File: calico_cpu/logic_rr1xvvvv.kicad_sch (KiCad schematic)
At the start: 8 parts, among them U36 74HC08, U37 74HC08, U38 74HC283, U39 74HC283

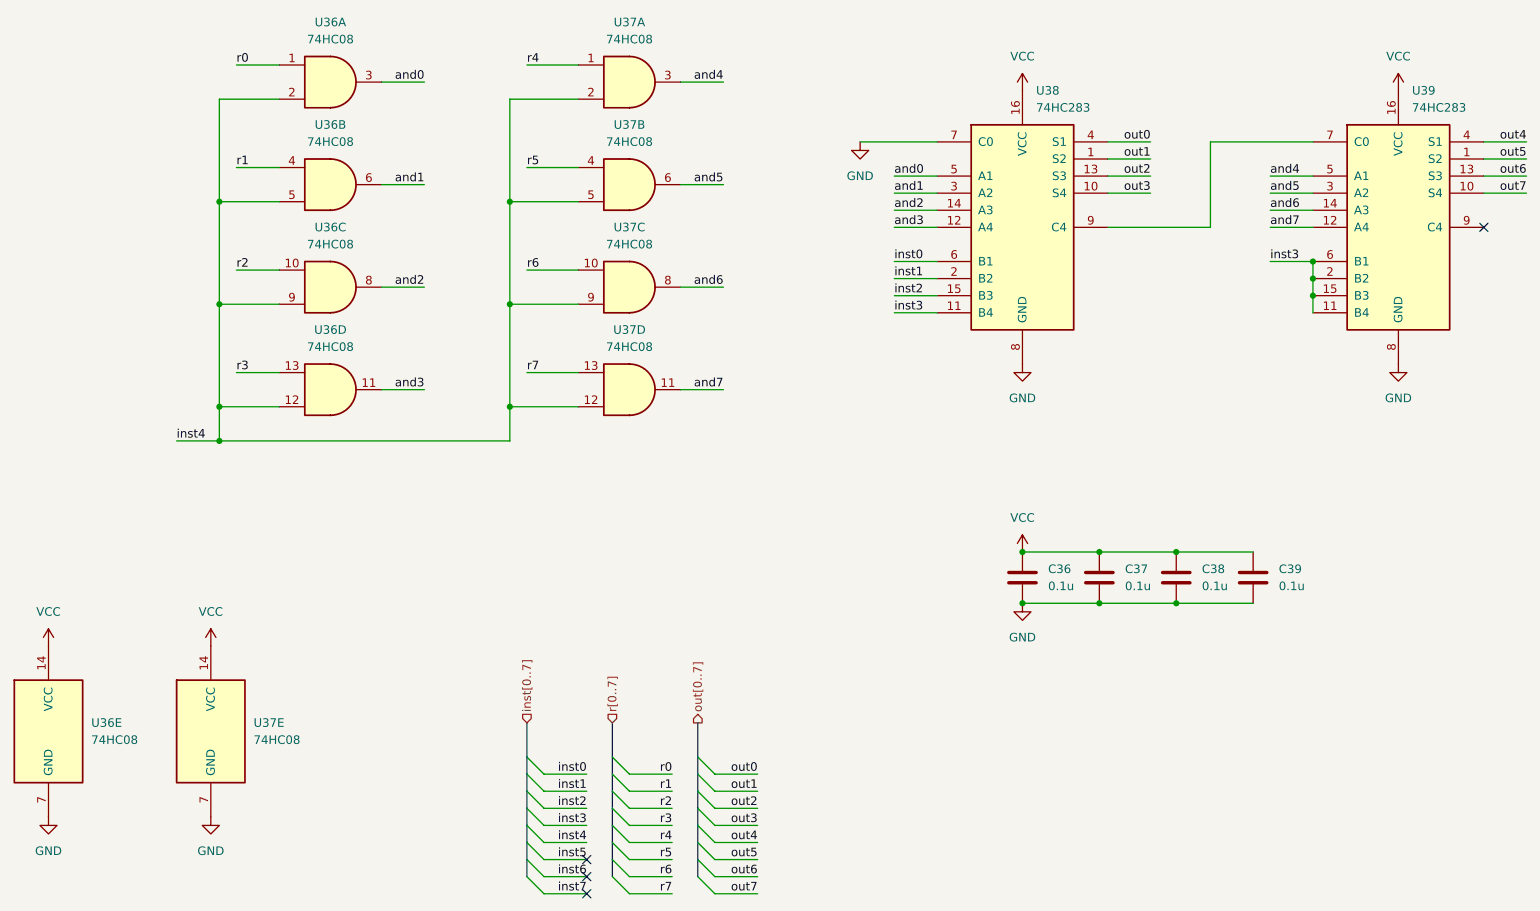
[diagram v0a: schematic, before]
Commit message: change "set immediate" to use zero-extend
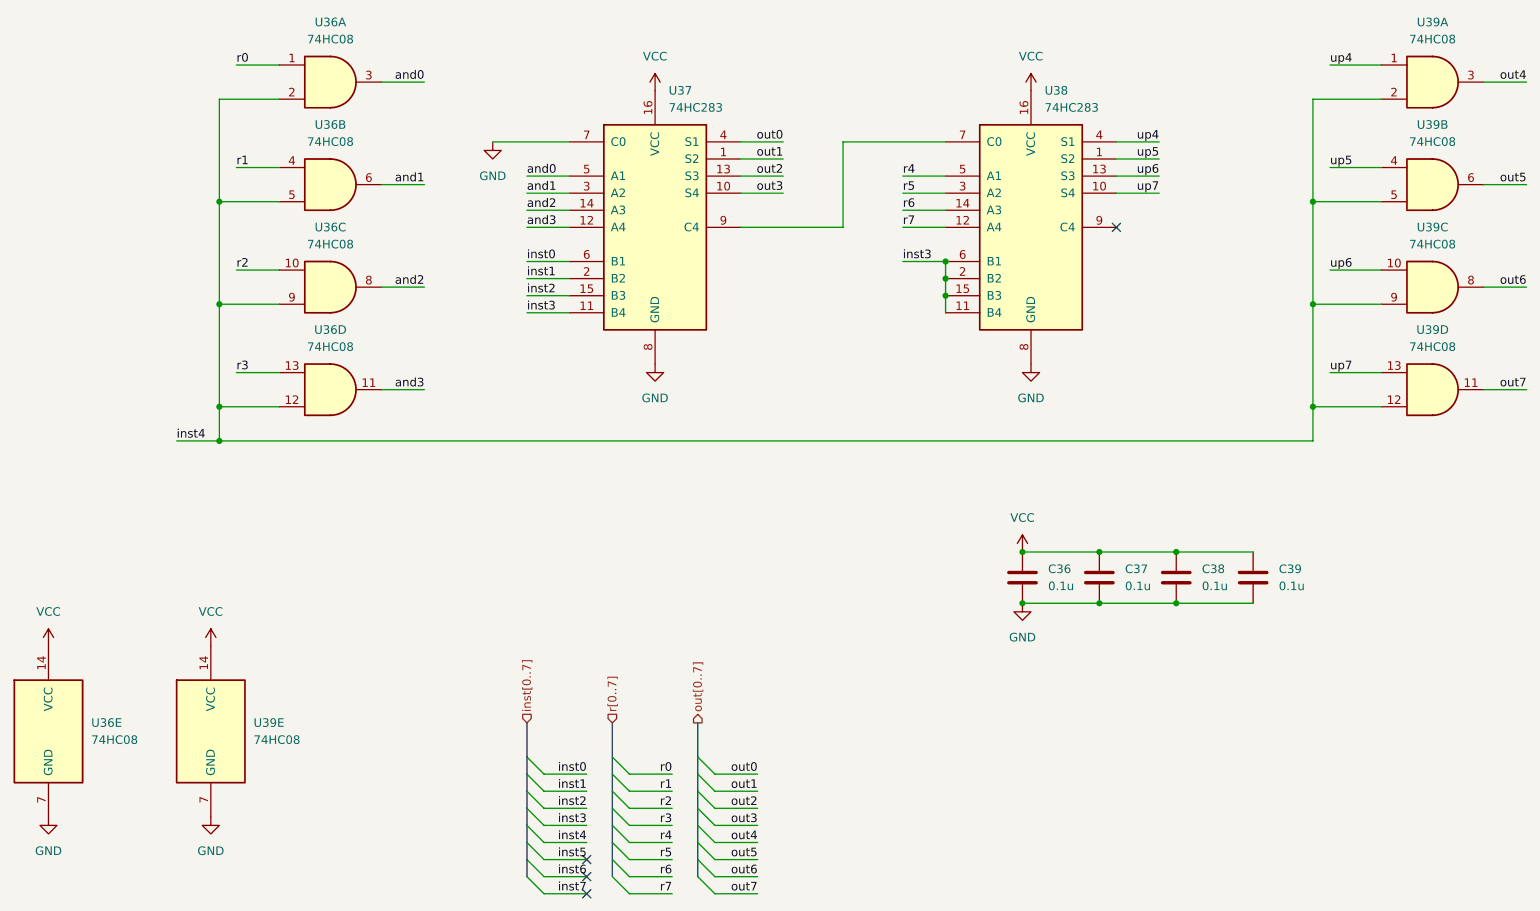
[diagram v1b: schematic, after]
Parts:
- renumbered U38 to U37, U39 to U38, U37 to U39
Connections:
- net out4: now also U39.3; no longer U38.4 (S1)
- net out5: now also U39.6; no longer U38.1 (S2)
- net out6: now also U39.8; no longer U38.13 (S3)
- net out7: now also U39.11; no longer U38.10 (S4)
- net r4: now also U38.5 (A1); no longer U39.1
- net r5: now also U38.3 (A2); no longer U39.4
- net r6: now also U38.14 (A3); no longer U39.10
- net r7: now also U38.12 (A4); no longer U39.13
- removed net and4: U38.5 (A1), U39.3
- removed net and5: U38.3 (A2), U39.6
- removed net and6: U38.14 (A3), U39.8
- removed net and7: U38.12 (A4), U39.11
- new net up4: U38.4 (S1), U39.1
- new net up5: U38.1 (S2), U39.4
- new net up6: U38.13 (S3), U39.10
- new net up7: U38.10 (S4), U39.13
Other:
- moved on the sheet: U37, U38, U39A, U39B, U39C, U39D

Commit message: calico_cpu: assign footprints
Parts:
- C36, C37, C38, C39: footprint (none) -> Capacitor_SMD:C_0805_2012Metric_Pad1.18x1.45mm_HandSolder
- U36, U39: footprint (none) -> PrjLibrary:DIP-14_W7.62mm_D1mm
- U37, U38: footprint (none) -> PrjLibrary:DIP-16_W7.62mm_D1mm
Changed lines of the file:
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@@
     (property "Reference" "U39" (id 0) (at 247.65 90.17 0))
     (property "Value" "74HC08" (id 1) (at 247.65 92.71 0))
-    (property "Footprint" "" (id 2) (at 247.65 99.06 0)
+    (property "Footprint" "PrjLibrary:DIP-14_W7.62mm_D1mm" (id 2) (at 247.65 99.06 0)
       (effects (font (size 1.27 1.27)) hide)
     )
@@
       (effects (font (size 1.27 1.27)) (justify left))
     )
-    (property "Footprint" "" (id 2) (at 199.0852 146.05 0)
+    (property "Footprint" "Capacitor_SMD:C_0805_2012Metric_Pad1.18x1.45mm_HandSolder" (id 2) (at 199.0852 146.05 0)
       (effects (font (size 1.27 1.27)) hide)
     )
@@
       (effects (font (size 1.27 1.27)) (justify left))
     )
-    (property "Footprint" "" (id 2) (at 221.9452 146.05 0)
+    (property "Footprint" "Capacitor_SMD:C_0805_2012Metric_Pad1.18x1.45mm_HandSolder" (id 2) (at 221.9452 146.05 0)
       (effects (font (size 1.27 1.27)) hide)
     )
@@
       (effects (font (size 1.27 1.27)) (justify left))
     )
-    (property "Footprint" "" (id 2) (at 187.6552 146.05 0)
+    (property "Footprint" "Capacitor_SMD:C_0805_2012Metric_Pad1.18x1.45mm_HandSolder" (id 2) (at 187.6552 146.05 0)
       (effects (font (size 1.27 1.27)) hide)
     )
@@
       (effects (font (size 1.27 1.27)) (justify left))
     )
-    (property "Footprint" "" (id 2) (at 66.04 165.1 0)
+    (property "Footprint" "PrjLibrary:DIP-14_W7.62mm_D1mm" (id 2) (at 66.04 165.1 0)
       (effects (font (size 1.27 1.27)) hide)
     )
@@
       (effects (font (size 1.27 1.27)) (justify left))
     )
-    (property "Footprint" "" (id 2) (at 132.08 90.17 0)
+    (property "Footprint" "PrjLibrary:DIP-16_W7.62mm_D1mm" (id 2) (at 132.08 90.17 0)
       (effects (font (size 1.27 1.27)) hide)
     )
@@
     (property "Reference" "U39" (id 0) (at 247.65 74.93 0))
     (property "Value" "74HC08" (id 1) (at 247.65 77.47 0))
-    (property "Footprint" "" (id 2) (at 247.65 83.82 0)
+    (property "Footprint" "PrjLibrary:DIP-14_W7.62mm_D1mm" (id 2) (at 247.65 83.82 0)
       (effects (font (size 1.27 1.27)) hide)
     )
@@
       (effects (font (size 1.27 1.27)) (justify left))
     )
-    (property "Footprint" "" (id 2) (at 210.5152 146.05 0)
+    (property "Footprint" "Capacitor_SMD:C_0805_2012Metric_Pad1.18x1.45mm_HandSolder" (id 2) (at 210.5152 146.05 0)
       (effects (font (size 1.27 1.27)) hide)
     )
@@
     (property "Reference" "U36" (id 0) (at 83.82 59.69 0))
     (property "Value" "74HC08" (id 1) (at 83.82 62.23 0))
-    (property "Footprint" "" (id 2) (at 83.82 68.58 0)
+    (property "Footprint" "PrjLibrary:DIP-14_W7.62mm_D1mm" (id 2) (at 83.82 68.58 0)
       (effects (font (size 1.27 1.27)) hide)
     )
@@
     (property "Reference" "U36" (id 0) (at 83.82 74.93 0))
     (property "Value" "74HC08" (id 1) (at 83.82 77.47 0))
-    (property "Footprint" "" (id 2) (at 83.82 83.82 0)
+    (property "Footprint" "PrjLibrary:DIP-14_W7.62mm_D1mm" (id 2) (at 83.82 83.82 0)
       (effects (font (size 1.27 1.27)) hide)
     )
@@
     (property "Reference" "U36" (id 0) (at 83.82 90.17 0))
     (property "Value" "74HC08" (id 1) (at 83.82 92.71 0))
-    (property "Footprint" "" (id 2) (at 83.82 99.06 0)
+    (property "Footprint" "PrjLibrary:DIP-14_W7.62mm_D1mm" (id 2) (at 83.82 99.06 0)
       (effects (font (size 1.27 1.27)) hide)
     )
@@
     (property "Reference" "U36" (id 0) (at 83.82 105.41 0))
     (property "Value" "74HC08" (id 1) (at 83.82 107.95 0))
-    (property "Footprint" "" (id 2) (at 83.82 114.3 0)
+    (property "Footprint" "PrjLibrary:DIP-14_W7.62mm_D1mm" (id 2) (at 83.82 114.3 0)
       (effects (font (size 1.27 1.27)) hide)
     )
@@
       (effects (font (size 1.27 1.27)) (justify left))
     )
-    (property "Footprint" "" (id 2) (at 41.91 165.1 0)
+    (property "Footprint" "PrjLibrary:DIP-14_W7.62mm_D1mm" (id 2) (at 41.91 165.1 0)
       (effects (font (size 1.27 1.27)) hide)
     )
@@
       (effects (font (size 1.27 1.27)) (justify left))
     )
-    (property "Footprint" "" (id 2) (at 187.96 90.17 0)
+    (property "Footprint" "PrjLibrary:DIP-16_W7.62mm_D1mm" (id 2) (at 187.96 90.17 0)
       (effects (font (size 1.27 1.27)) hide)
     )
@@
     (property "Reference" "U39" (id 0) (at 247.65 105.41 0))
     (property "Value" "74HC08" (id 1) (at 247.65 107.95 0))
-    (property "Footprint" "" (id 2) (at 247.65 114.3 0)
+    (property "Footprint" "PrjLibrary:DIP-14_W7.62mm_D1mm" (id 2) (at 247.65 114.3 0)
       (effects (font (size 1.27 1.27)) hide)
     )
@@
     (property "Reference" "U39" (id 0) (at 247.65 59.69 0))
     (property "Value" "74HC08" (id 1) (at 247.65 62.23 0))
-    (property "Footprint" "" (id 2) (at 247.65 68.58 0)
-      (effects (font (size 1.27 1.27)) hide)
-    )
+    (property "Footprint" "PrjLibrary:DIP-14_W7.62mm_D1mm" (id 2) (at 247.65 68.58 0)
+      (effects (font (size 1.27 1.27)) hide)
+    )
